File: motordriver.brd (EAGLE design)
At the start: 101.3 x 82.5 mm, 99 parts, among them J1 CONNECTOR_MOTORS, J10 HEADER_1X3, J11 HEADER_1X3, J2 CONNECTOR_MOTORS, J3 CONNECTOR_MOTORS, J4 CONNECTOR_MOTORS, J5 HEADER_1X3, J6 HEADER_1X3, J7 HEADER_1X3, J8 HEADER_1X3, J9 CONNECTOR_MOTORS, Q1 MOSFET, Q10 MOSFET, Q11 MOSFET, Q12 MOSFET, Q13 MOSFET, Q14 MOSFET, Q15 MOSFET, Q16 MOSFET, Q2 MOSFET, Q3 MOSFET, Q4 MOSFET, Q5 MOSFET, Q6 MOSFET, Q7 MOSFET, Q8 MOSFET, Q9 MOSFET, U1 74XX139_PDIP, U10 IR2111_PDIP, U11 IR2111_PDIP, U12 7812_TO220, U2 TL084_PDIP, U3 7812_TO220, U4 IR2111_PDIP, U5 IR2111_PDIP, U6 IR2111_PDIP, U7 IR2111_PDIP, U8 IR2111_PDIP, U9 IR2111_PDIP

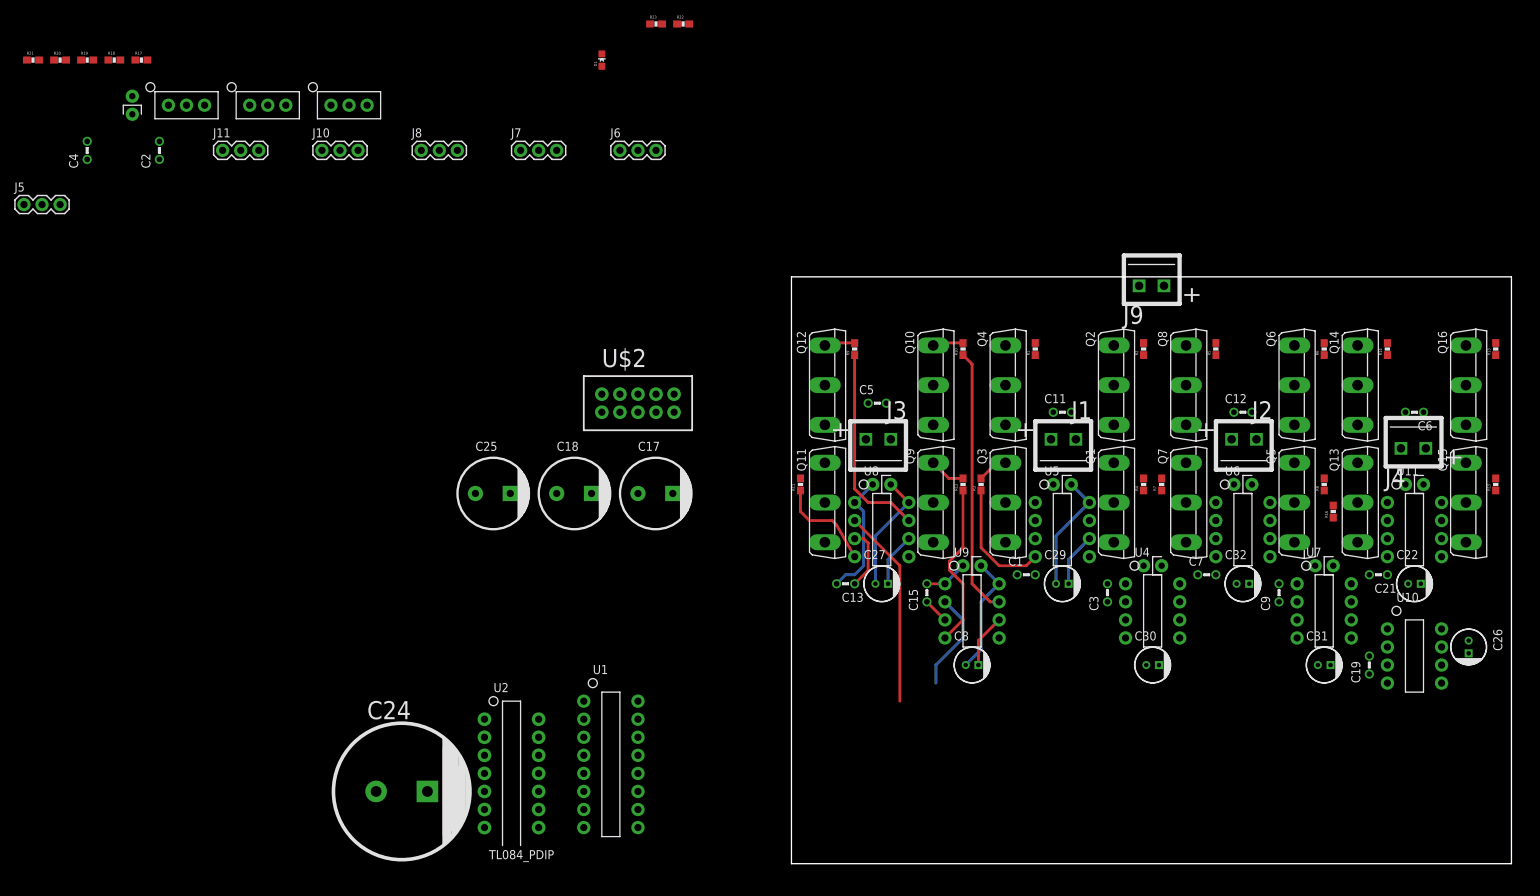
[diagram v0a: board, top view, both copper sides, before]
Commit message: Components arranged, 86'ed the 36V cap (fit ext.)
YEEEEEHAA it all fits. I will still be rearranging components, but
initially they all fit. Routing will happen later this afternoon.
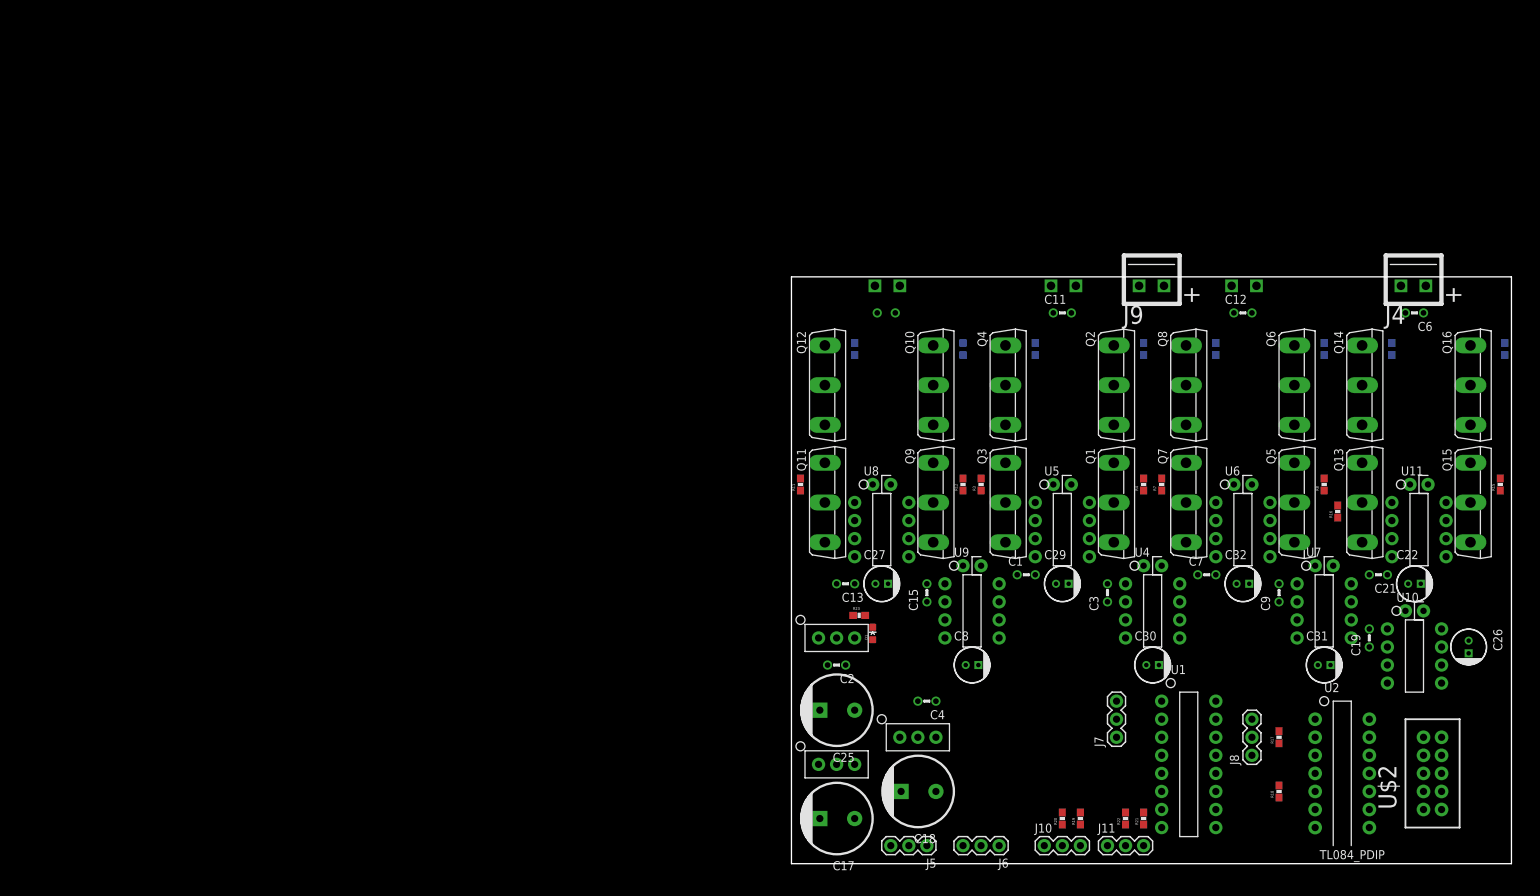
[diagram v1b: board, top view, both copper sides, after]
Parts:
- removed C24: CAP_2200U_63V, motordriverslib:RADIAL_18
- moved R18 193.4 mm to (68.6, 10.2), turned to 90 degrees
- moved D7 193.1 mm to (86.4, 35.6), turned to 90 degrees
- moved R21 189.2 mm to (49.5, 6.35), turned to 90 degrees
- moved R17 186.2 mm to (68.6, 17.8), turned to 90 degrees
- moved R20 176.8 mm to (38.1, 6.35), turned to 90 degrees
- moved R19 175.8 mm to (40.6, 6.35), turned to 90 degrees
- moved J11 158.3 mm to (47.0, 2.54)
- moved J5 151.6 mm to (16.5, 2.54), turned to 180 degrees
- moved C4 141.6 mm to (20.3, 22.9), turned to 90 degrees
- moved J10 141.0 mm to (38.1, 2.54)
- moved J8 141.0 mm to (64.8, 17.8), turned to 90 degrees
- moved U12 130.2 mm to (6.35, 14.0)
- moved R22 127.9 mm to (47.0, 6.35), turned to 90 degrees
- moved U$2 123.3 mm to (90.2, 12.7), turned to 90 degrees
- moved C2 119.9 mm to (7.62, 27.9), turned to 90 degrees
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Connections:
- net GND: no longer C24.-
- net VCC_12V: no longer C24.+
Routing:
- net N$3: track 37.6 -> 0.00 mm
- net N$28: track 28.3 -> 0.00 mm
- net X_PWM_B: track 28.0 -> 0.00 mm
- net VCC_12V: track 24.0 -> 0.00 mm
- net N$1: track 23.4 -> 0.00 mm
- net N$20: track 17.2 -> 0.00 mm
- net N$47: track 17.0 -> 0.00 mm
- net N$13: track 17.0 -> 0.00 mm
- net N$55: track 17.0 -> 0.00 mm
- net X_PWM_A: track 14.1 -> 0.00 mm
- net N$29: track 13.9 -> 0.00 mm
- net GND: track 12.3 -> 0.00 mm
- net N$48: track 7.56 -> 0.00 mm
- net N$15: track 7.56 -> 0.00 mm
- net N$56: track 7.56 -> 0.00 mm
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
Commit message: Routing Adventure Part I
Its never ogre.
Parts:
- moved U2 34.9 mm to (39.4, 26.7)
- moved R18 26.5 mm to (43.2, 17.8), flipped to the bottom, turned to 270 degrees
- moved R17 25.9 mm to (43.2, 22.9), flipped to the bottom
- moved J6 16.6 mm to (10.2, 1.27)
- moved J5 14.9 mm to (2.54, 7.62), turned to 90 degrees
- moved J7 11.5 mm to (57.1, 19.1)
- moved C4 10.9 mm to (29.2, 16.5)
- moved U1 10.2 mm to (62.2, 21.6)
- moved U$2 9.25 mm to (81.3, 10.2), turned to 270 degrees
- moved J8 8.98 mm to (73.7, 16.5)
- moved U$1 8.98 mm to (26.7, 19.1)
- moved C18 8.89 mm to (29.2, 10.2)
- moved C25 6.87 mm to (14.6, 25.4), turned to 270 degrees
- moved J2 6.35 mm to (69.8, 81.3)
- moved C17 5.46 mm to (12.1, 10.8), turned to 0 degrees
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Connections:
- net GND renamed GND_32
- net VCC_12V: now also U$1.IN
- net V_IN: no longer U$1.IN
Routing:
- net V_IN: track 0.00 -> 143.6 mm
- net VCC_5V: track 0.00 -> 103.6 mm
- net VCC_12V: track 0.00 -> 93.0 mm
- net X_PWM_B: track 0.00 -> 57.6 mm
- net Y_A: track 0.00 -> 48.0 mm
- net X_B: track 0.00 -> 48.0 mm
- net X_A: track 0.00 -> 46.8 mm
- net N$3: track 0.00 -> 38.4 mm
- net Y_B: track 0.00 -> 38.1 mm
- net N$51: track 0.00 -> 36.6 mm
- net N$54: track 0.00 -> 35.8 mm
- net Y_PWM_A_RAW: track 0.00 -> 35.4 mm
- net X_PWM_A: track 0.00 -> 33.9 mm
- net GND_32: track 0.00 -> 31.0 mm
- net VCC_12V_ALT: track 0.00 -> 29.6 mm
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- added copper zone on layer 16, net GND_32

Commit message: PCB Routing the Trilogy Part II
SO MUCH TO DO SO MUCH TO SEE
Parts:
- moved C30 10.8 mm to (58.4, 35.6), turned to 270 degrees
- moved R5 5.85 mm to (65.4, 71.1)
- moved C7 3.59 mm to (59.7, 38.1), turned to 0 degrees
- moved C26 2.54 mm to (97.8, 30.5)
- moved D7 2.54 mm to (88.9, 35.6)
- moved U10 2.54 mm to (86.4, 33.0)
- moved C21 2.54 mm to (83.8, 38.1), turned to 0 degrees
- moved D14 2.54 mm to (47.0, 41.9)
- moved J2 2.54 mm to (67.3, 81.3)
- moved C22 1.27 mm to (88.9, 39.4)
- moved C19 1.27 mm to (81.3, 31.8)
- moved D12 1.27 mm to (61.0, 53.3)
- moved D13 1.27 mm to (72.4, 41.9)
- moved D15 1.27 mm to (35.6, 53.3)
- moved R1 1.27 mm to (34.3, 71.1)
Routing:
- net VCC_12V: track 93.0 -> 212.2 mm, vias 0 -> 1
- net Y_PWM_B: track 0.00 -> 80.8 mm, vias 0 -> 1
- net X_PWM_B: track 57.6 -> 115.6 mm, vias 0 -> 1
- net Y_PWM_A: track 0.00 -> 41.3 mm
- net N$40: track 0.00 -> 37.9 mm
- net N$27: track 0.00 -> 36.8 mm, vias 0 -> 2
- net N$18: track 13.9 -> 41.6 mm
- net N$34: track 13.9 -> 39.8 mm
- net N$16: track 0.00 -> 25.2 mm
- net N$2: track 0.00 -> 24.6 mm
- net N$19: track 0.00 -> 23.6 mm
- net N$21: track 13.8 -> 37.1 mm
- net N$32: track 0.00 -> 23.2 mm
- net N$37: track 13.8 -> 35.5 mm
- net N$30: track 0.00 -> 19.0 mm
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
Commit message: TIS FUCKING DONE
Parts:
- moved C26 11.7 mm to (90.2, 21.6), turned to 0 degrees
- moved C13 3.59 mm to (6.35, 41.9), turned to 180 degrees
- moved C19 2.84 mm to (83.8, 30.5)
- moved D7 2.54 mm to (86.4, 35.6)
- moved D9 1.27 mm to (85.7, 53.3)
- moved R13 0.90 mm to (99.7, 71.8)
- moved R14 0.64 mm to (84.5, 71.8)
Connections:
- removed net VIN_RAW: J9.+, U3.IN
- net V_IN: now also J9.+, U3.IN
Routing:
- net X_PWM_A: track 33.9 -> 98.4 mm
- net N$66: track 0.00 -> 44.8 mm
- net VCC_12V: track 212.2 -> 254.6 mm, vias 1 -> 2
- net N$9: track 0.00 -> 33.4 mm
- net N$71: track 14.5 -> 43.0 mm
- net N$74: track 0.00 -> 25.8 mm
- net N$68: track 13.8 -> 36.2 mm
- net N$64: track 0.00 -> 20.3 mm
- net N$72: track 0.00 -> 19.4 mm
- net V_IN: track 143.6 -> 160.1 mm
- net VIN_RAW: track 15.6 -> 0.00 mm
- net N$65: track 0.00 -> 8.30 mm
- net N$73: track 0.00 -> 7.67 mm
- net N$76: track 0.00 -> 5.72 mm
- net N$77: track 0.00 -> 5.19 mm
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
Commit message: PCB sweep up, Part III of the 8 part Penilogy
Yeah
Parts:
- moved C21 4.26 mm to (81.9, 41.9), turned to 180 degrees
- moved C7 3.59 mm to (57.1, 40.6), turned to 270 degrees
- moved C1 2.84 mm to (33.0, 40.6), turned to 180 degrees
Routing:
- net VCC_12V: track 254.6 -> 258.1 mm
- added copper zone on layer 1, net GND_32

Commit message: SHIP IT!
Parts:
- moved C21 3.57 mm to (82.2, 38.4), turned to 0 degrees
- moved C2 3.06 mm to (9.91, 27.4)
- moved D1 3.06 mm to (13.1, 31.9)
- moved U3 3.06 mm to (7.37, 30.0)
- moved R23 3.06 mm to (10.5, 33.8)
- moved C31 2.79 mm to (74.9, 25.1)
- moved C8 2.54 mm to (25.4, 25.4)
- moved C26 2.54 mm to (90.2, 19.1)
- moved U12 2.41 mm to (7.37, 15.7)
- moved J6 2.34 mm to (11.9, 2.79)
- moved D15 2.03 mm to (35.6, 55.4)
- moved C29 1.78 mm to (38.1, 37.6)
- moved U7 1.78 mm to (71.1, 37.6)
- moved U9 1.78 mm to (21.6, 37.6)
- moved C15 1.52 mm to (19.1, 35.3)
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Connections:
- removed net N$6: R23.1
- net GND_32: now also R23.1
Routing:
- net VCC_12V: track 258.1 -> 264.8 mm
- net VCC_12V_ALT: track 29.6 -> 23.5 mm
- net N$38: track 18.2 -> 23.1 mm
- net N$13: track 18.3 -> 21.6 mm
- net N$55: track 18.2 -> 21.4 mm
- net N$64: track 20.3 -> 23.3 mm
- net V_IN: track 160.1 -> 162.7 mm
- net GND_32: track 31.0 -> 28.7 mm, vias 0 -> 7
- net N$47: track 18.0 -> 20.1 mm
- net N$56: track 7.56 -> 9.36 mm
- net N$15: track 8.51 -> 10.2 mm
- net N$40: track 37.9 -> 39.5 mm
- net N$39: track 7.56 -> 9.02 mm
- net N$48: track 8.30 -> 9.44 mm
- net REF_3V: track 22.4 -> 23.5 mm
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
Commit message: Front side labels...COMPLETE
IT tAkes AlOT of COoKs to mAke A STew.
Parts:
- renumbered U$2 to ENC

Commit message: Final Design, SHIPPED
Complete
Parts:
- moved J8 1.02 mm to (72.6, 16.5)
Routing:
- net Y_IN: track 3.81 -> 2.79 mm
- net Y_EN: track 3.81 -> 2.79 mm
- net Y_DIR: track 3.81 -> 2.79 mm
- net GND_32: vias 7 -> 64
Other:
- board text added: "+"
- board text added: "-"
- board text added: "12V"
- board text added: "5V"
- board text added: "7805"
- board text added: "7812"
- board text added: "A"
- board text added: "B"
- board text added: "DIR"
- board text added: "EN"
- board text added: "GND"
- board text added: "IN"
- board text added: "TDFW DEERTAYBRD REV 0.0.0.0.1"
- board text added: "X"
- board text added: "X:A"
- board text added: "X:B"
- board text added: "X:DIR"
- board text added: "X:EN"
- board text added: "X:IN"
- board text added: "Y"
- board text added: "Y:A"
- board text added: "Y:B"
